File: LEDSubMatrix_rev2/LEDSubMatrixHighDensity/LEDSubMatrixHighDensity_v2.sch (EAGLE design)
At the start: 154 parts, among them IC1 TLC5955DCAR, IC10 SN74LVC1G34DBVR, IC11 SN74LVC1G34DBVR, IC2 TLC5955DCAR, IC3 TLC5955DCAR, IC4 TLC5955DCAR, IC5 TLC5955DCAR, IC6 TLC5955DCAR, IC7 TLC5955DCAR, IC8 TLC5955DCAR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

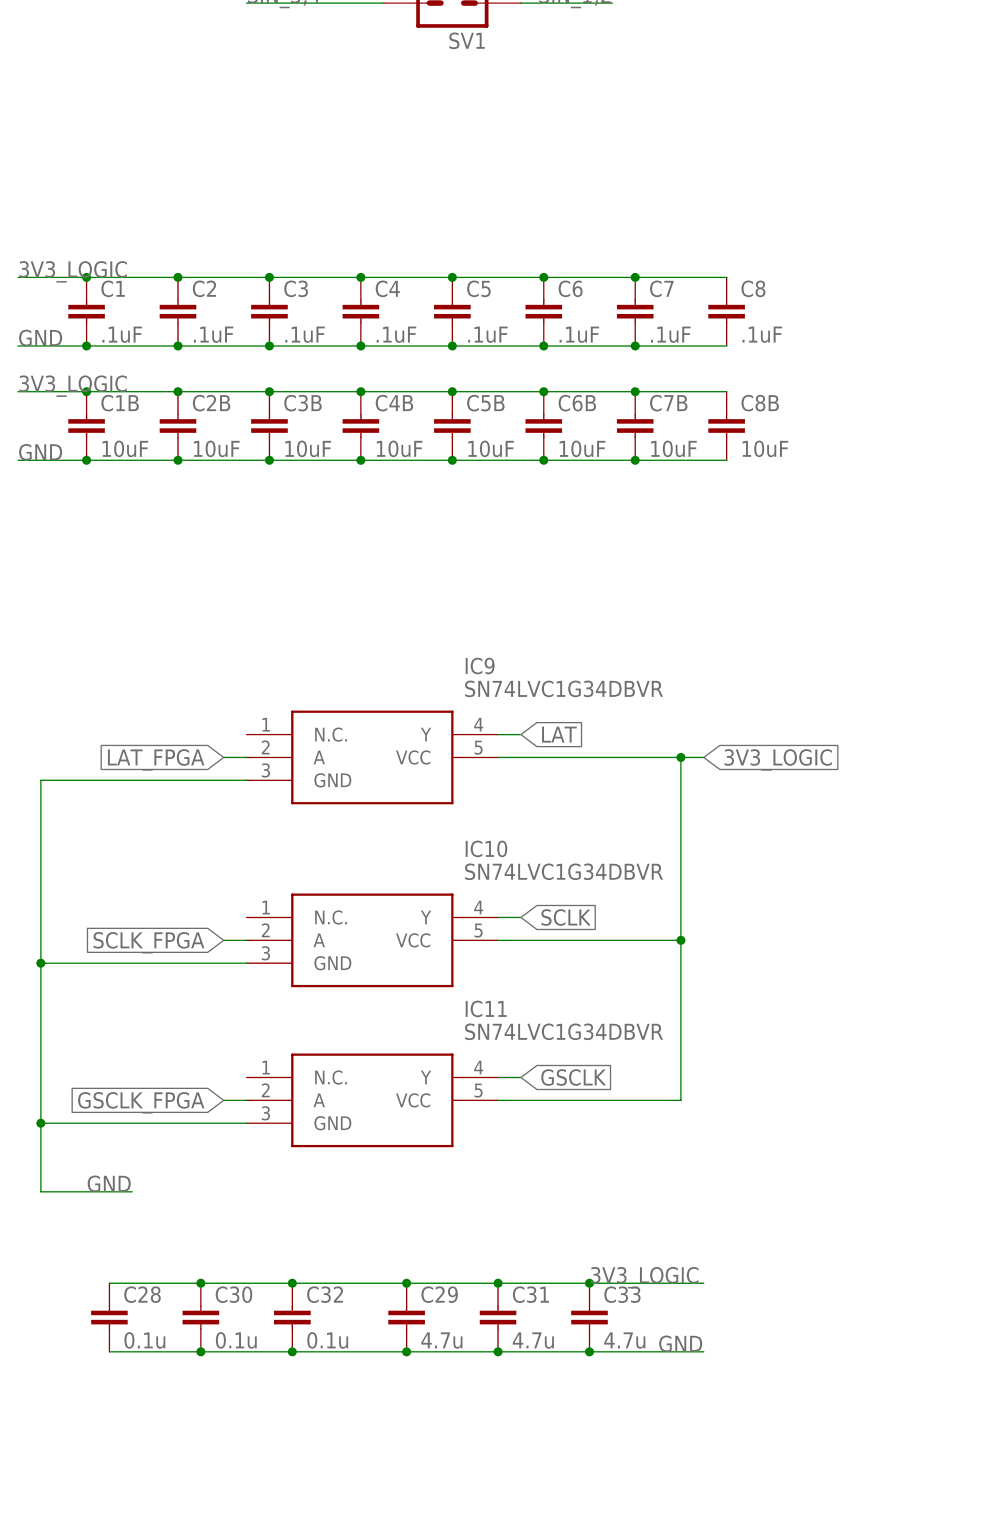
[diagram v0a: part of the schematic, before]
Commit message: fixed soldermask on led submatrix
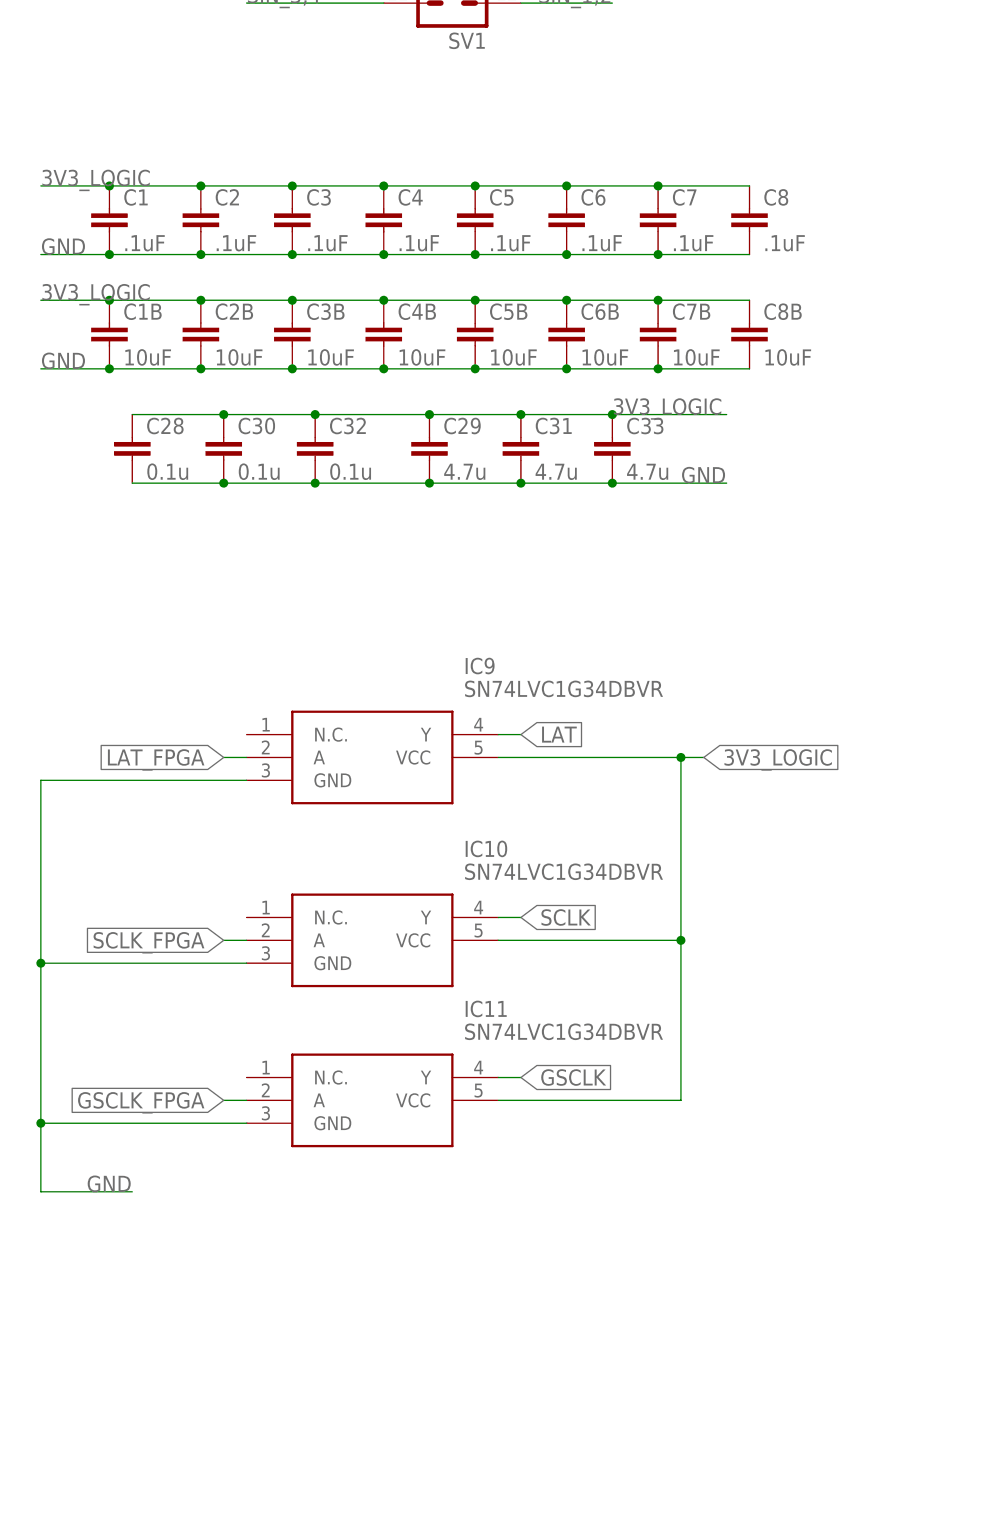
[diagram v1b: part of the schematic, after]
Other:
- moved on the sheet: C1, C1B, C2, C28, C29, C2B, C3, C30, C31, C32, C33, C3B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
